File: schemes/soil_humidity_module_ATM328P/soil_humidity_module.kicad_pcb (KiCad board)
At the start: 4 copper layers, 47 x 48.9 mm, 30 parts, among them J1 Conn_01x03, Q1 IRL540N, Q2 BC547, U1 NRF24L01_Breakout, U2 SEN0193, U3 LD1117S33TR_SOT223, U4 ATmega328P-PU, Y1 16MHz

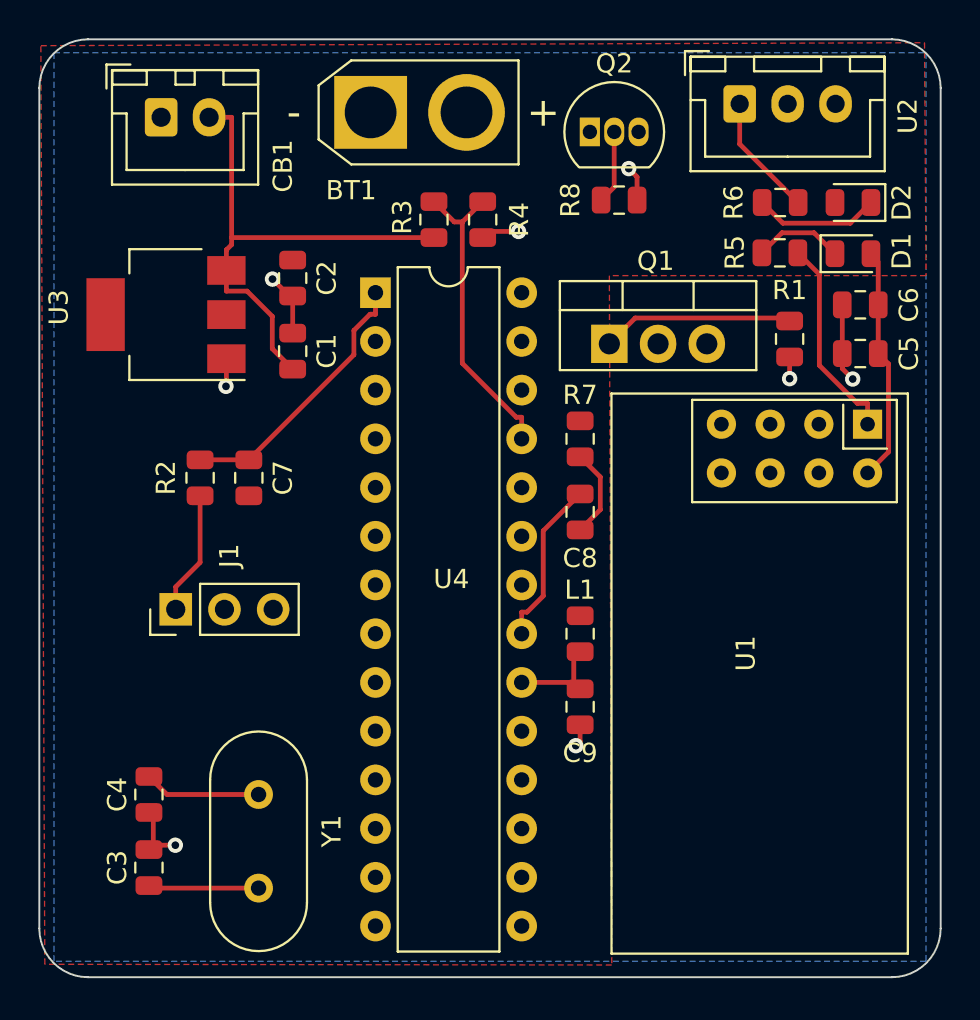
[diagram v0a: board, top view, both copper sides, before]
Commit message: [android_app] Relay settings working
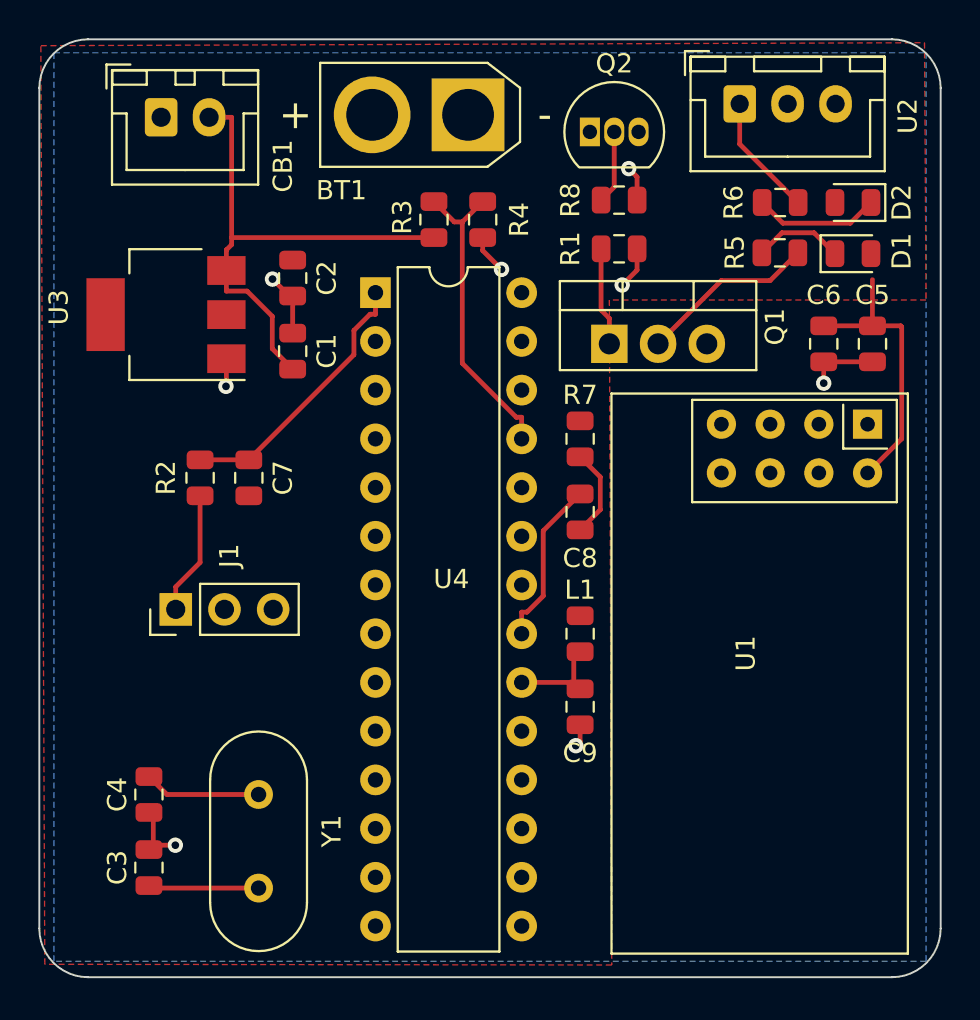
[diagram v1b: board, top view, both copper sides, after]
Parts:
- moved R1 10.1 mm to (158.5, 90.9), turned to 0 degrees
- moved BT1 5.08 mm to (150.6, 83.9), turned to 180 degrees
- moved C6 2.79 mm to (169.2, 95.9), turned to 270 degrees
- moved C5 0.81 mm to (171.7, 95.9), turned to 270 degrees
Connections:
- BT1 pad 1: Net-(BT1-Pad1) -> GND
- BT1 pad 2: GND -> Net-(BT1-Pad1)
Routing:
- net Q1_D4: track 27.0 -> 22.1 mm
- net +3V3: track 11.7 -> 14.8 mm
- net Net-(Q1-Pad2): track 23.5 -> 22.0 mm
- net GND: track 18.3 -> 19.0 mm

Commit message: [soil_humidity_transmitter] Switching to internal 8MHz on ATMega
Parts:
- R2: value 10k -> 1k
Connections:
- net Net-(C1-Pad1) renamed VCC

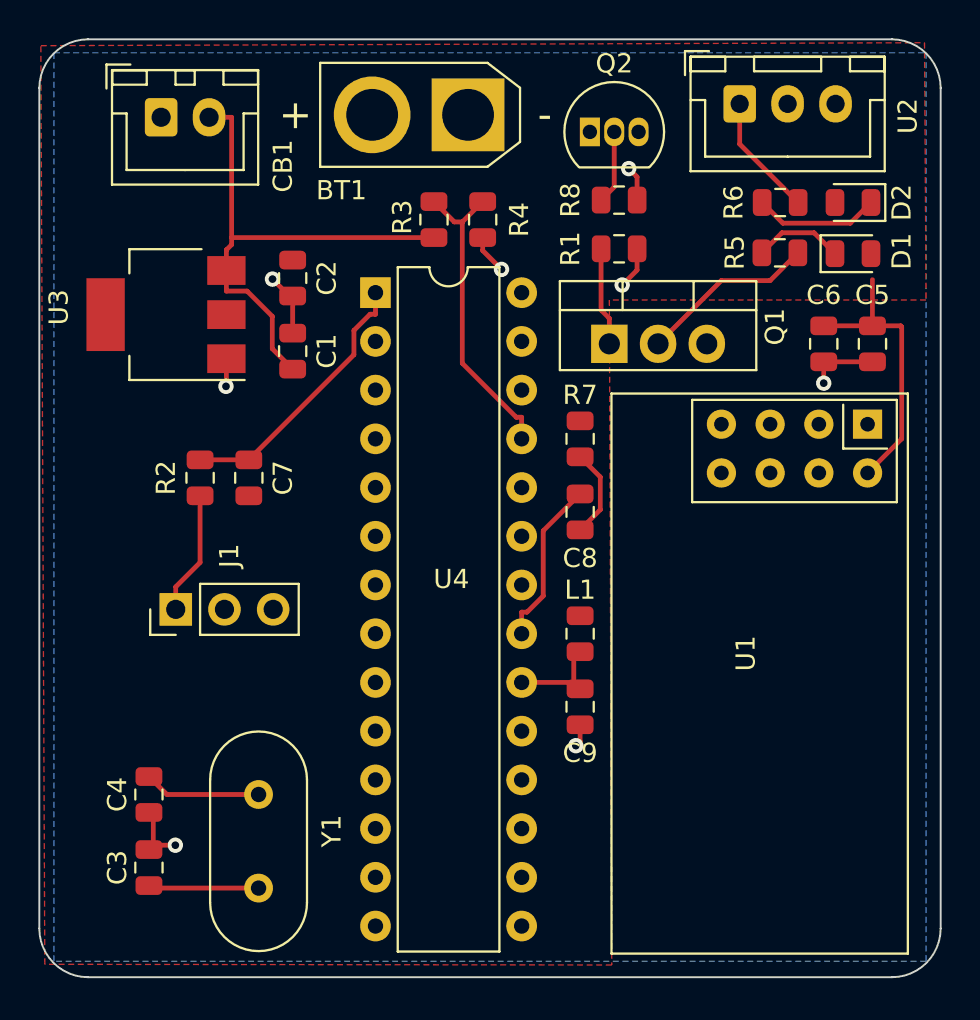
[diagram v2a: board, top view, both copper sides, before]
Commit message: [soil_humidity_transmitter] Using the watchdog to wake up the uC
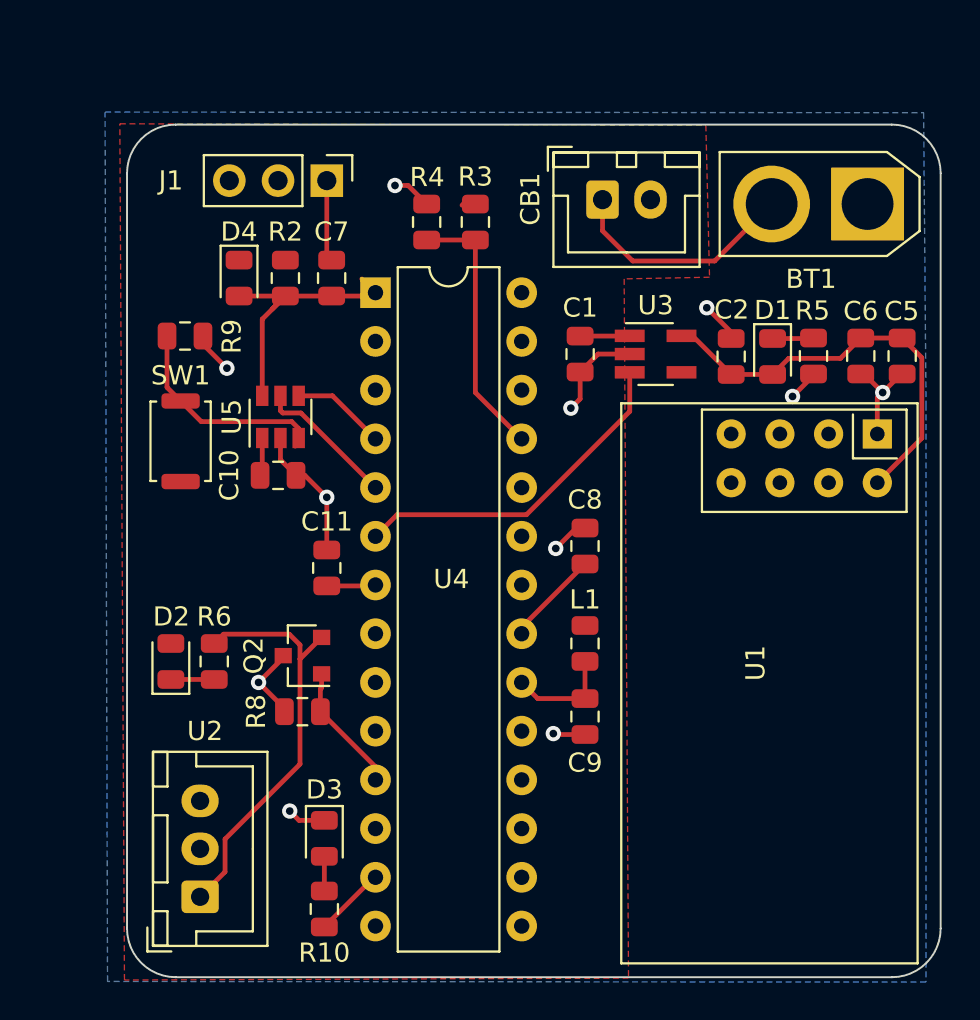
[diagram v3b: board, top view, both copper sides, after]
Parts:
- removed C3, C4: 22pF, Capacitor_SMD:C_0805_2012Metric
- removed Q1: IRL540N, Package_TO_SOT_THT:TO-220-3_Vertical
- removed R1: 1M, Resistor_SMD:R_0805_2012Metric
- removed R7: 3.2k, Resistor_SMD:R_0805_2012Metric
- removed Y1: 16MHz, Crystal:Crystal_HC49-4H_Vertical
- added C10: 100nF, Capacitor_SMD:C_0805_2012Metric, F.Cu at (140.7, 102.7)
- added C11: 100nF, Capacitor_SMD:C_0805_2012Metric, F.Cu at (143.3, 107.6)
- added D3: LED_ALT, LED_SMD:LED_0805_2012Metric, F.Cu at (143.1, 121.7)
- added D4: 1N4148, Diode_SMD:D_0805_2012Metric, F.Cu at (138.7, 92.5)
- added R10: 1k, Resistor_SMD:R_0805_2012Metric, F.Cu at (143.1, 125.3)
- added R9: 170k, Resistor_SMD:R_0805_2012Metric, F.Cu at (135.9, 95.5)
- added SW1: SW_Push, Button_Switch_SMD:SW_Push_SPST_NO_Alps_SKRK, F.Cu at (135.6, 101.0)
- added U5: TPL5010, Package_TO_SOT_SMD:SOT-23-6, F.Cu at (140.8, 99.7)
- C1: value 100nF -> 1uF
- C2: value 10uF -> 1uF
- Q2: value BC547 -> DMG6968U; footprint Package_TO_SOT_THT:TO-92_Inline -> Package_TO_SOT_SMD:SOT-23
- R2: value 1k -> 10k
- U3: value LD1117S33TR_SOT223 -> AP7365; footprint Package_TO_SOT_SMD:SOT-223-3_TabPin2 -> Package_TO_SOT_SMD:SOT-23-5_HandSoldering
- moved U2 50.0 mm to (136.7, 124.7), turned to 90 degrees
- moved D2 42.9 mm to (135.1, 112.4), turned to 90 degrees
- moved R6 38.0 mm to (137.4, 112.4), turned to 90 degrees
- moved R8 31.4 mm to (142.0, 115.1), turned to 180 degrees
- moved Q2 31.1 mm to (142.0, 112.1), turned to 180 degrees
- moved U3 25.6 mm to (160.4, 96.4), turned to 0 degrees
- moved J1 23.7 mm to (143.3, 87.4), turned to 270 degrees
- moved CB1 23.4 mm to (157.6, 88.4)
- moved C2 23.2 mm to (164.3, 96.5), turned to 90 degrees
- moved BT1 21.3 mm to (171.4, 88.6)
- moved C1 15.0 mm to (156.5, 96.4), turned to 270 degrees
- moved C7 12.5 mm to (143.5, 92.5), turned to 90 degrees
- moved R2 10.6 mm to (141.1, 92.5)
- moved D1 6.80 mm to (166.5, 96.5), turned to 270 degrees
- moved R5 5.66 mm to (168.6, 96.5), turned to 270 degrees
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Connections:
- C7 pad 1: Net-(C7-Pad1) -> U5_RST
- C8 pad 2: Net-(C8-Pad2) -> GND
- D2 pad 2: +3V3 -> VCC
- L1 pad 1: +3V3 -> VCC
- Q2 pad 1: Net-(Q2-Pad1) -> Q2_D5
- Q2 pad 2: Q2_D5 -> Net-(Q2-Pad2)
- R2 pad 1: +3V3 -> U5_RST
- R2 pad 2: Net-(C7-Pad1) -> VCC
- R5 pad 2: Net-(Q1-Pad2) -> GND
- R6 pad 2: Net-(Q2-Pad1) -> Net-(Q2-Pad2)
- U1 pad 1: Net-(Q1-Pad2) -> GND
- U2 pad 1: Net-(Q2-Pad1) -> Net-(Q2-Pad2)
- U2 pad 2: +3V3 -> VCC
- U3 pad 1: GND -> VCC
- U3 pad 2: +3V3 -> GND
- U3 pad 3: VCC -> Q1_D4
- U4 pad 1: Net-(C7-Pad1) -> U5_RST
- U4 pad 21: Net-(C8-Pad2) -> Net-(C8-Pad1)
- U4 pad 4: Net-(U4-Pad4) -> U5_D2
- U4 pad 5: Net-(U4-Pad5) -> U5_D3
- U4 pad 7: +3V3 -> VCC
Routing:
- net Q2_D5: track 43.2 -> 6.74 mm
- net Net-(Q1-Pad2): track 22.0 -> 0.00 mm
- net Net-(Q2-Pad2): track 0.00 -> 21.8 mm
- net VCC: track 27.0 -> 7.81 mm
- net GND: track 19.0 -> 36.0 mm, vias 8 -> 11
- net Net-(U4-Pad10): track 16.6 -> 0.00 mm
- net Net-(Q2-Pad1): track 15.5 -> 0.00 mm
- net U5_RST: track 0.00 -> 15.4 mm
- net Net-(U4-Pad9): track 15.1 -> 0.00 mm
- net Net-(C7-Pad1): track 14.2 -> 0.00 mm
- net Net-(R9-Pad1): track 0.00 -> 11.4 mm
- net Net-(C8-Pad2): track 8.71 -> 0.00 mm
- net U5_D3: track 0.00 -> 8.05 mm
- net +3V3: track 14.8 -> 22.1 mm
- net RXD_J1: track 17.4 -> 10.5 mm
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- added copper zone on F.Cu, net VCC
- removed copper zone on F.Cu, net +3V3
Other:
- board size 47 x 48.9 mm -> 42.4 x 44.5 mm
